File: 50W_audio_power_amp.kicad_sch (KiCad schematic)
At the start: 15 parts, among them IC1 OPA454AIDDAR, Q1 2SCR586D3, Q2 2SAR586D3

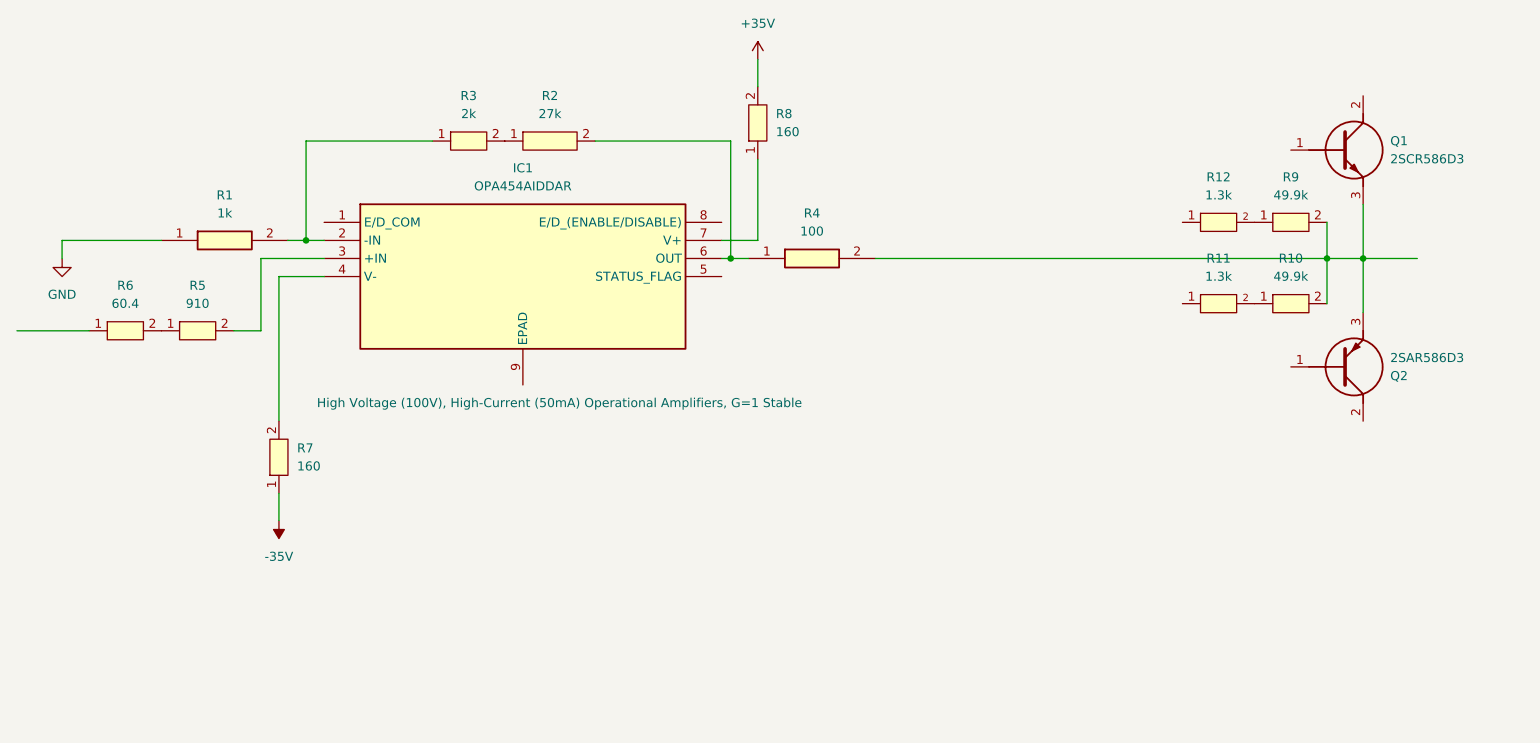
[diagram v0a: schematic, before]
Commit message: Added schematic version and titles
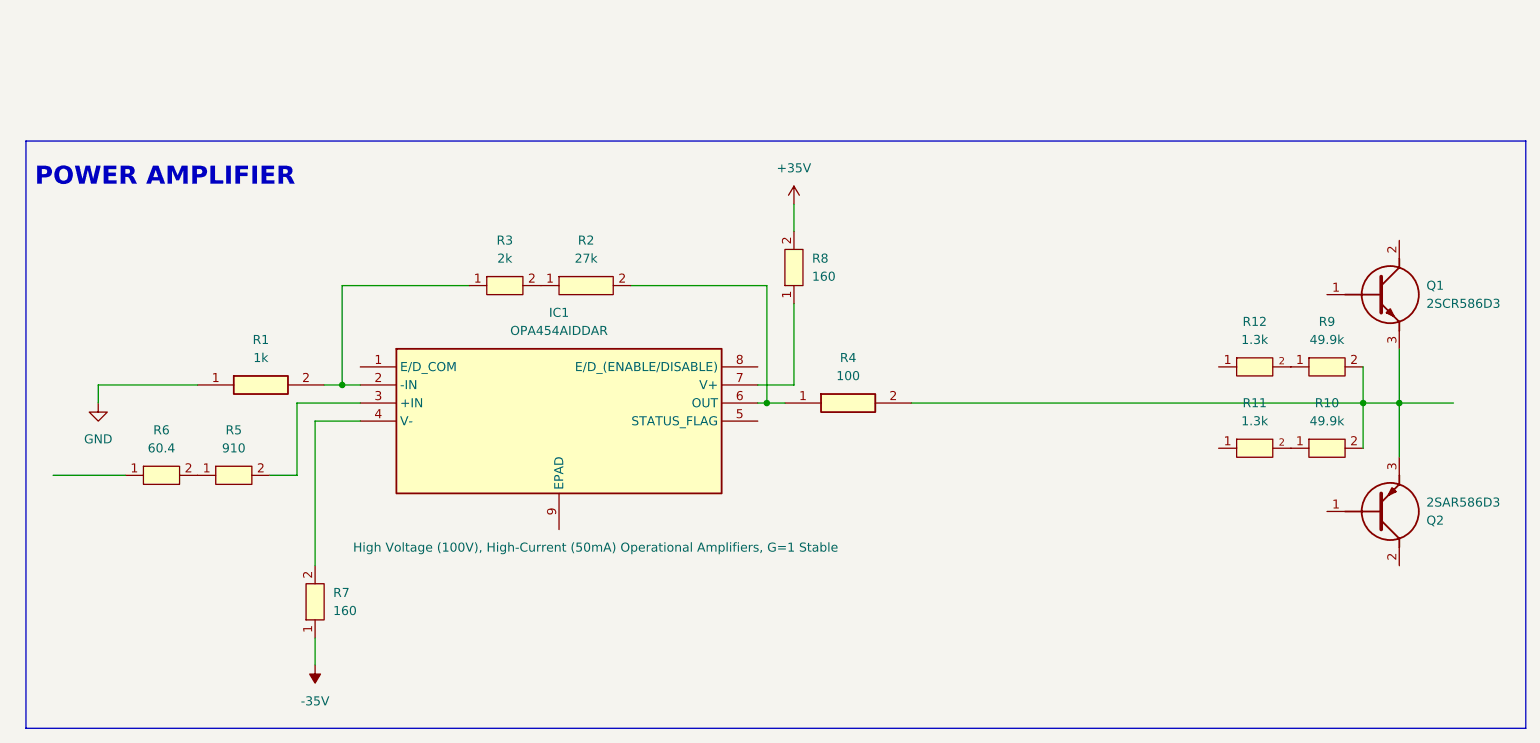
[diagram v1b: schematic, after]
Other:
- note added: "POWER AMPLIFIER"
- title: (none) -> POWER SUPPLY & AUDIO POWER AMP
- moved on the sheet: IC1, Q1, Q2, R1, R10, R11, R12, R2, R3, R4, R5, R6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
